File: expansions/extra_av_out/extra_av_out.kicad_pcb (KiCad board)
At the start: 4 copper layers, 76.3 x 88.1 mm, 53 parts, among them J1 Conn_02x25_Odd_Even, J2 SJ1-3533NG, J3 PLT133/T10W, J4 VGA, Q1 BC847, U1 ADV7125KSTZ140, U2 PCM5142PW, U3 74HCT2G17GW

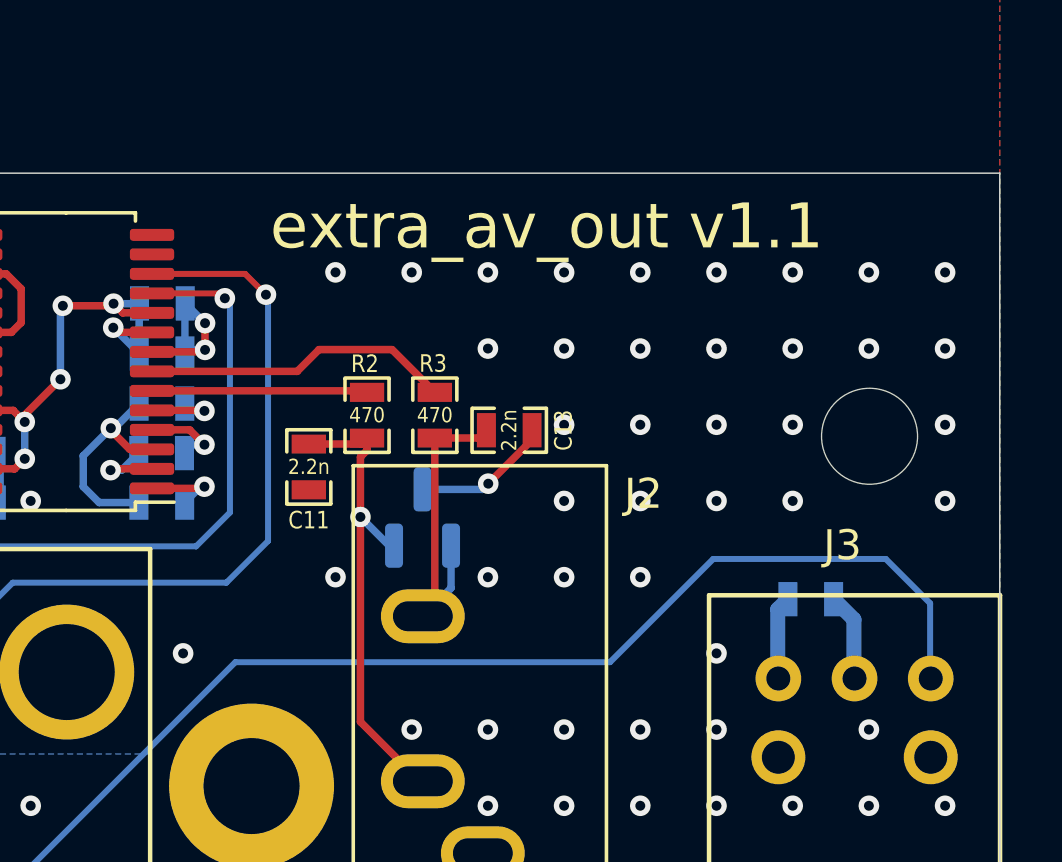
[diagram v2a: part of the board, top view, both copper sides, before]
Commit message: update extra_av_out to v1.2
* fix Toslink footprint pin order
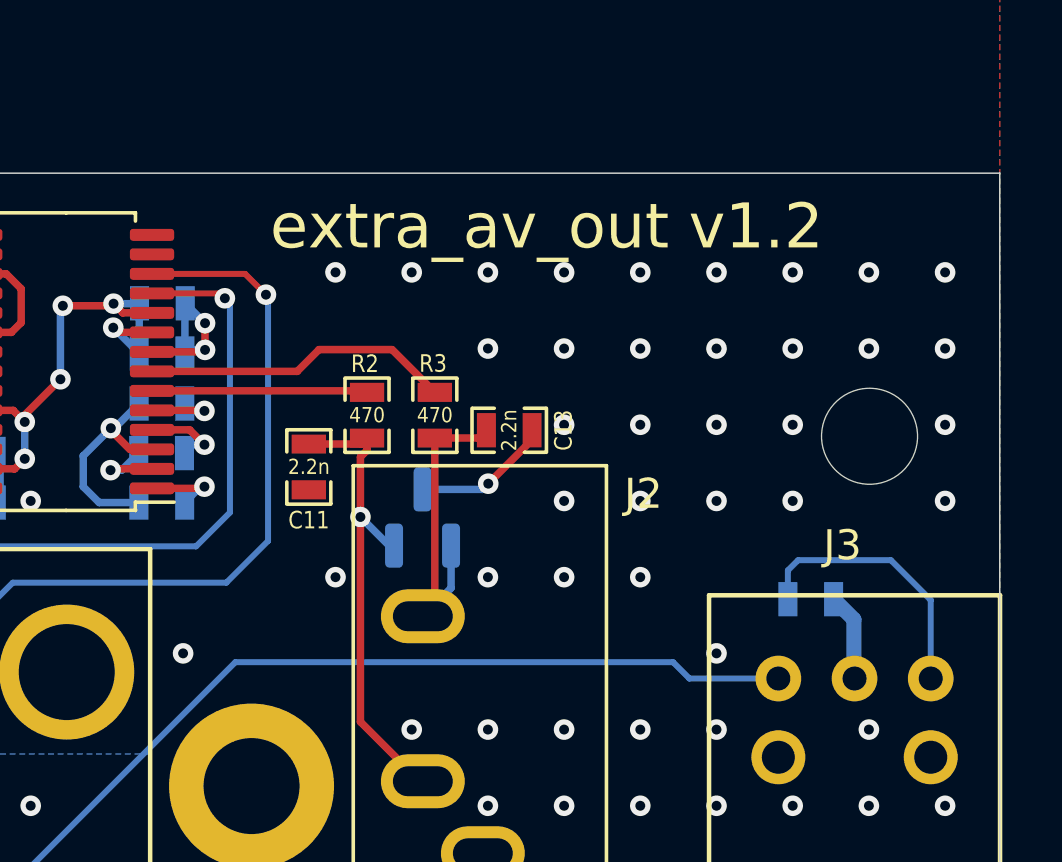
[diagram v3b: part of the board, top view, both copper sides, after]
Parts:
- J3: footprint custom_components:EAPLRAA4 -> custom_components:PLT133
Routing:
- net /SPDIF: track 90.3 -> 81.0 mm
- net GND: track 104.4 -> 110.9 mm
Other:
- board text added: "extra_av_out v1.2"
- board text removed: "extra_av_out v1.1"
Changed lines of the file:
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@@
     )
   )
-  (footprint "custom_components:EAPLRAA4" (layer "F.Cu")
+  (footprint "custom_components:PLT133" (layer "F.Cu")
     (at 115 76.345 180)
     (property "Sheetfile" "extra_av_out.kicad_sch")
@@
     (property "ki_keywords" "connector")
     (attr through_hole)
-    (fp_text reference "J3" (at 0.40132 4.43992) (layer "F.SilkS")
-        (effects (font (size 1 1) (thickness 0.15)))
-    )
-    (fp_text value "PLT133/T10W" (at -0.1143 -4.51358) (layer "F.Fab")
+    (fp_text reference "J3" (at 0.40132 4.43992 180) (layer "F.SilkS")
+        (effects (font (size 1 1) (thickness 0.15)))
+    )
+    (fp_text value "PLT133/T10W" (at -0.1143 -4.51358 180) (layer "F.Fab")
         (effects (font (size 1 1) (thickness 0.15)))
     )
@@
     (fp_line (start 4.85 2.775) (end -4.85 2.775)
       (stroke (width 0.15) (type solid)) (layer "F.SilkS"))
-    (pad "1" thru_hole circle (at -2.54 0 180) (size 1.524 1.524) (drill 0.8) (layers "*.Cu" "*.Mask")
+    (pad "1" thru_hole circle (at 2.54 0 180) (size 1.524 1.524) (drill 0.8) (layers "*.Cu" "*.Mask")
       (net 14 "/SPDIF") (pinfunction "Pin_1") (pintype "passive"))
     (pad "2" thru_hole circle (at 0 0 180) (size 1.524 1.524) (drill 0.8) (layers "*.Cu" "*.Mask")
       (net 2 "/DVDD3v3") (pinfunction "Pin_2") (pintype "passive"))
-    (pad "3" thru_hole circle (at 2.54 0 180) (size 1.524 1.524) (drill 0.8) (layers "*.Cu" "*.Mask")
+    (pad "3" thru_hole circle (at -2.54 0 180) (size 1.524 1.524) (drill 0.8) (layers "*.Cu" "*.Mask")
       (net 1 "GND") (pinfunction "Pin_3") (pintype "passive"))
     (pad "4" thru_hole circle (at 2.54 -2.625 180) (size 1.8 1.8) (drill 1.1) (layers "*.Cu" "*.Mask"))
@@
       (net 56 "/VGA_VS_TTL") (pinfunction "IO2") (pintype "passive"))
     (pad "4" smd rect (at 0.85 -0.54 180) (size 0.5 0.38) (layers "B.Cu" "B.Paste" "B.Mask")
-      (net 60 "unconnected-(D2-IO3-Pad4)") (pinfunction "IO3") (pintype "passive"))
+      (net 60 "unconnected-(D2-IO3-Pad4)") (pinfunction "IO3") (pintype "passive+no_connect"))
     (pad "5" smd rect (at 0.85 0.54 180) (size 0.5 0.38) (layers "B.Cu" "B.Paste" "B.Mask")
-      (net 61 "unconnected-(D2-IO4-Pad5)") (pinfunction "IO4") (pintype "passive"))
+      (net 61 "unconnected-(D2-IO4-Pad5)") (pinfunction "IO4") (pintype "passive+no_connect"))
     (model "${KICAD6_3DMODEL_DIR}/Package_TO_SOT_SMD.3dshapes/SOT-665.wrl"
       (offset (xyz 0 0 0))
@@
   (gr_line (start 119.84 83.5) (end 119.84 59.5)
     (stroke (width 0.05) (type solid)) (layer "Edge.Cuts"))
-  (gr_text "extra_av_out v1.1" (at 104.74 61.28) (layer "F.SilkS")
+  (gr_text "extra_av_out v1.2" (at 104.74 61.28) (layer "F.SilkS")
     (effects (font (size 1.5 1.5) (thickness 0.3)))
   )
@@
   (segment (start 64.85 53.62) (end 64.85 54.94) (width 0.25) (layer "B.Cu") (net 1))
   (segment (start 86.394 68.87) (end 86.384 68.86) (width 0.5) (layer "B.Cu") (net 1))
-  (segment (start 112.44 74.038) (end 112.778 73.7) (width 0.5) (layer "B.Cu") (net 1))
   (segment (start 102.6 70.04) (end 102.79 69.85) (width 0.25) (layer "B.Cu") (net 1))
+  (segment (start 116.21 72.4) (end 113.12 72.4) (width 0.2) (layer "B.Cu") (net 1))
   (segment (start 63.74 76.13) (end 65.96 78.35) (width 0.25) (layer "B.Cu") (net 1))
+  (segment (start 113.12 72.4) (end 112.778 72.742) (width 0.2) (layer "B.Cu") (net 1))
   (segment (start 67.33 53.15) (end 67.458 53.15) (width 0.25) (layer "B.Cu") (net 1))
   (segment (start 100.6 70.04) (end 102.6 70.04) (width 0.25) (layer "B.Cu") (net 1))
@@
   (segment (start 89.29 68.92) (end 90.21 68) (width 0.25) (layer "B.Cu") (net 1))
   (segment (start 90.21 68) (end 90.33 68) (width 0.25) (layer "B.Cu") (net 1))
-  (segment (start 112.44 76.1) (end 112.44 74.038) (width 0.5) (layer "B.Cu") (net 1))
   (segment (start 87.34 69.022) (end 87.34 67.792) (width 0.25) (layer "B.Cu") (net 1))
   (segment (start 90.29 64.65) (end 90.296 64.65) (width 0.25) (layer "B.Cu") (net 1))
@@
   (segment (start 86.394 70.48) (end 86.394 68.87) (width 0.5) (layer "B.Cu") (net 1))
   (segment (start 89.82 70.48) (end 89.29 69.95) (width 0.25) (layer "B.Cu") (net 1))
+  (segment (start 117.52 76.325) (end 117.54 76.345) (width 0.2) (layer "B.Cu") (net 1))
   (segment (start 76.94 57.1) (end 76.94 58.17) (width 0.25) (layer "B.Cu") (net 1))
   (segment (start 70.75 59.42) (end 71.87 59.42) (width 0.25) (layer "B.Cu") (net 1))
   (segment (start 70.3 72.49) (end 71.4 73.59) (width 0.5) (layer "B.Cu") (net 1))
+  (segment (start 117.54 76.345) (end 117.54 73.73) (width 0.2) (layer "B.Cu") (net 1))
   (segment (start 55.08 77.37) (end 55.11 77.4) (width 0.5) (layer "B.Cu") (net 1))
+  (segment (start 112.778 72.742) (end 112.778 73.7) (width 0.2) (layer "B.Cu") (net 1))
   (segment (start 67.458 53.15) (end 67.968 53.66) (width 0.25) (layer "B.Cu") (net 1))
   (segment (start 65.96 78.35) (end 68.16 78.35) (width 0.25) (layer "B.Cu") (net 1))
+  (segment (start 117.54 73.73) (end 116.21 72.4) (width 0.2) (layer "B.Cu") (net 1))
   (segment (start 70.3 71.306) (end 70.3 72.49) (width 0.5) (layer "B.Cu") (net 1))
   (segment (start 89.29 69.95) (end 89.29 68.92) (width 0.25) (layer "B.Cu") (net 1))
@@
   (segment (start 50.77 81.966) (end 52.586 80.15) (width 0.2) (layer "F.Cu") (net 13))
   (segment (start 48.42579 88.20871) (end 47.66 87.44292) (width 0.2) (layer "F.Cu") (net 13))
+  (segment (start 57.03 83.04) (end 87.12 83.04) (width 0.2) (layer "B.Cu") (net 14))
+  (segment (start 94.36 75.8) (end 108.95 75.8) (width 0.2) (layer "B.Cu") (net 14))
+  (segment (start 54.84 89.97) (end 56.67 88.14) (width 0.2) (layer "B.Cu") (net 14))
   (segment (start 56.67 83.4) (end 57.03 83.04) (width 0.2) (layer "B.Cu") (net 14))
-  (segment (start 110.29 72.36) (end 116.04 72.36) (width 0.2) (layer "B.Cu") (net 14))
-  (segment (start 45.88579 85.66871) (end 44.53579 87.01871) (width 0.2) (layer "B.Cu") (net 14))
-  (segment (start 87.12 83.04) (end 94.36 75.8) (width 0.2) (layer "B.Cu") (net 14))
-  (segment (start 54.84 89.97) (end 56.67 88.14) (width 0.2) (layer "B.Cu") (net 14))
-  (segment (start 44.53579 87.01871) (end 44.53579 88.766252) (width 0.2) (layer "B.Cu") (net 14))
+  (segment (start 56.67 88.14) (end 56.67 83.4) (width 0.2) (layer "B.Cu") (net 14))
+  (segment (start 108.95 75.8) (end 109.495 76.345) (width 0.2) (layer "B.Cu") (net 14))
+  (segment (start 109.495 76.345) (end 112.46 76.345) (width 0.2) (layer "B.Cu") (net 14))
   (segment (start 44.53579 88.766252) (end 45.739538 89.97) (width 0.2) (layer "B.Cu") (net 14))
   (segment (start 45.739538 89.97) (end 54.84 89.97) (width 0.2) (layer "B.Cu") (net 14))
-  (segment (start 56.67 88.14) (end 56.67 83.4) (width 0.2) (layer "B.Cu") (net 14))
-  (segment (start 117.52 76.325) (end 117.54 76.345) (width 0.2) (layer "B.Cu") (net 14))
-  (segment (start 94.36 75.8) (end 106.85 75.8) (width 0.2) (layer "B.Cu") (net 14))
-  (segment (start 106.85 75.8) (end 110.29 72.36) (width 0.2) (layer "B.Cu") (net 14))
-  (segment (start 57.03 83.04) (end 87.12 83.04) (width 0.2) (layer "B.Cu") (net 14))
-  (segment (start 117.52 73.84) (end 117.52 76.325) (width 0.2) (layer "B.Cu") (net 14))
-  (segment (start 116.04 72.36) (end 117.52 73.84) (width 0.2) (layer "B.Cu") (net 14))
+  (segment (start 87.12 83.04) (end 94.36 75.8) (width 0.2) (layer "B.Cu") (net 14))
+  (segment (start 44.53579 87.01871) (end 44.53579 88.766252) (width 0.2) (layer "B.Cu") (net 14))
+  (segment (start 45.88579 85.66871) (end 44.53579 87.01871) (width 0.2) (layer "B.Cu") (net 14))
   (segment (start 84.407 66.107) (end 84.07 65.77) (width 0.2) (layer "F.Cu") (net 15))
   (segment (start 85.8575 66.107) (end 84.815 66.107) (width 0.2) (layer "F.Cu") (net 15))
